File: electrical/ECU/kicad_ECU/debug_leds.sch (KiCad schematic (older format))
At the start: 6 parts

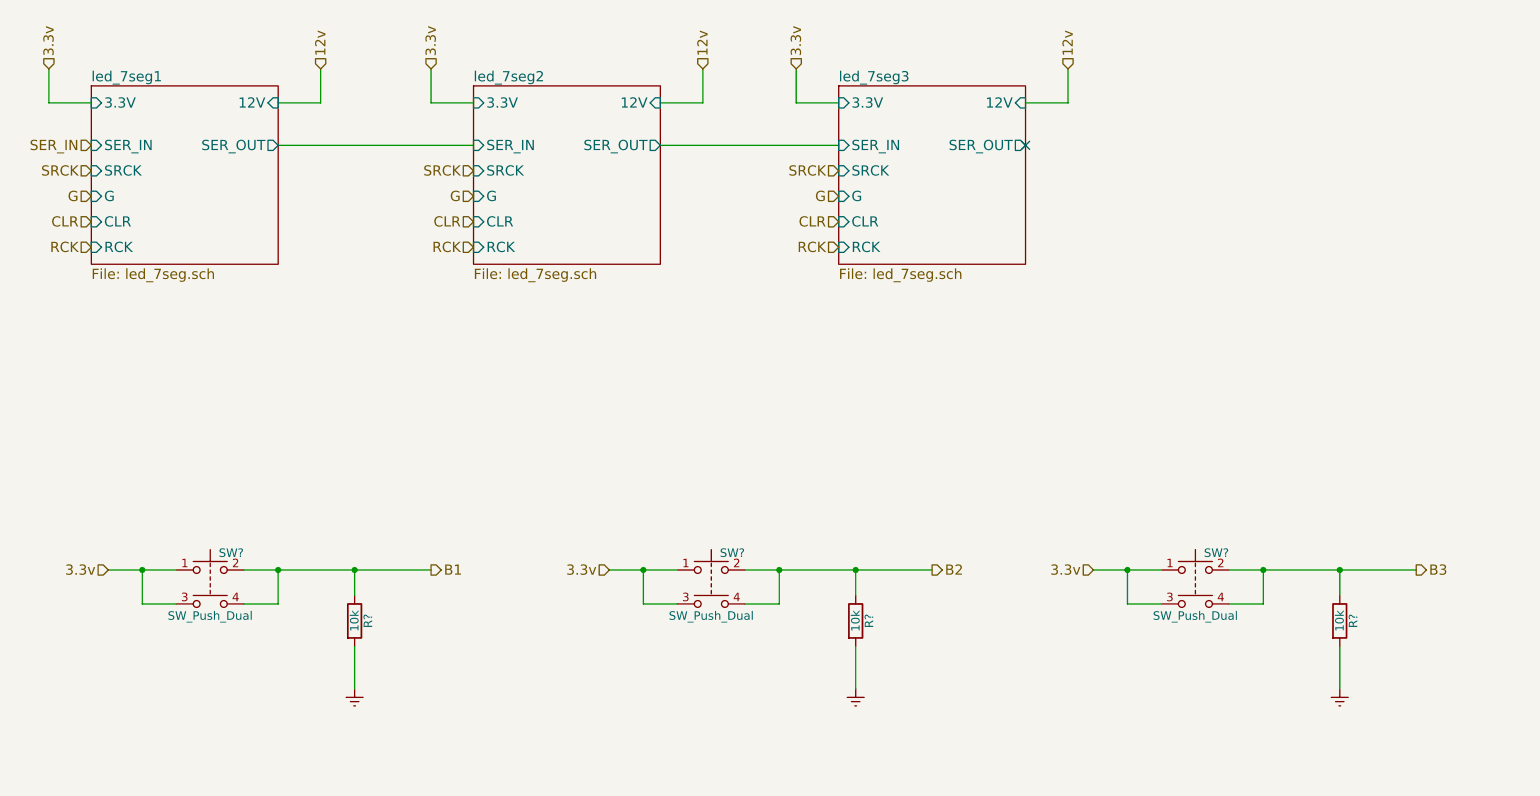
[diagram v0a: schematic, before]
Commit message: fixed some naming errors and initial round of double checking
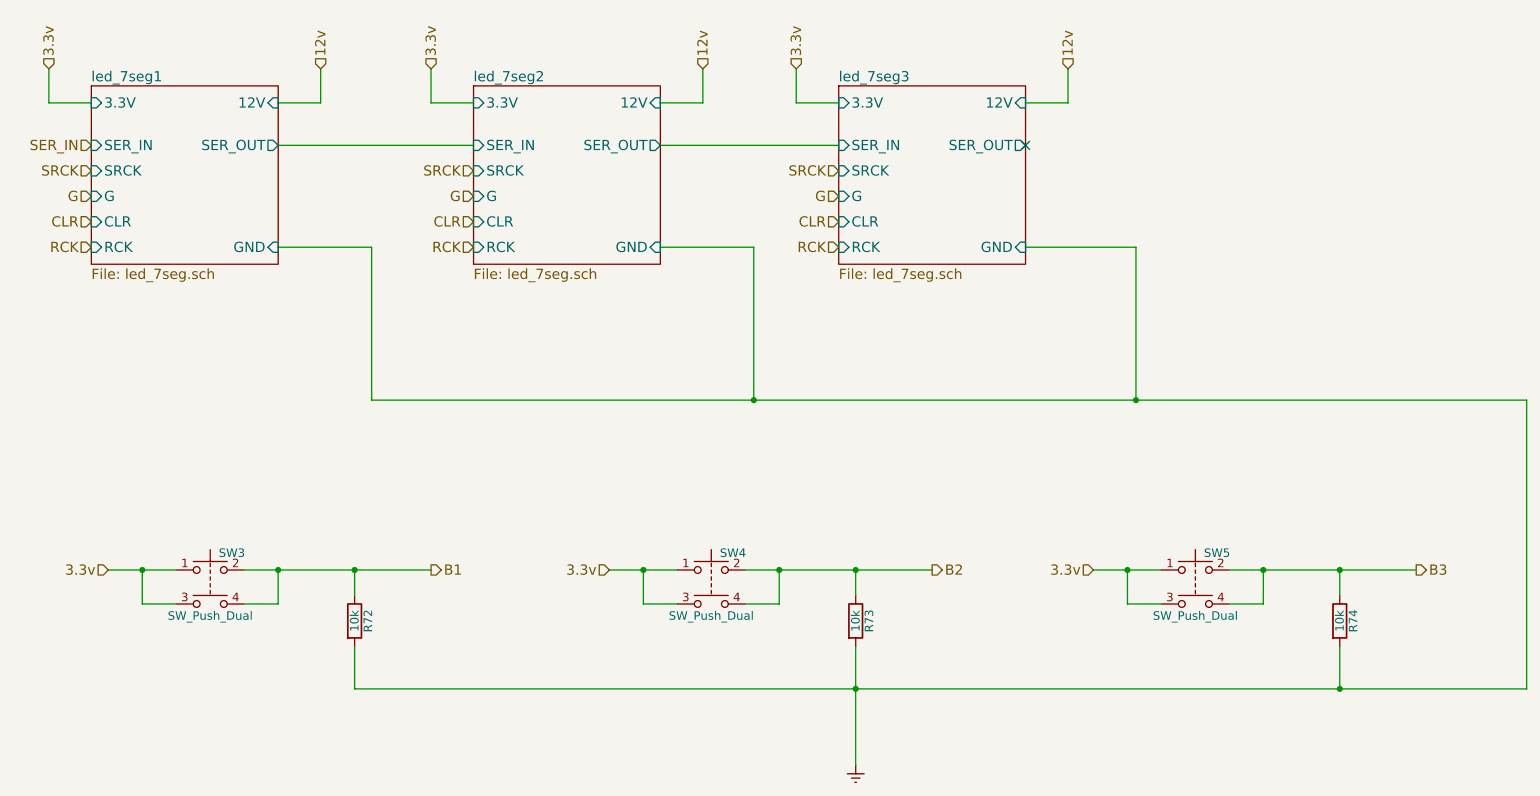
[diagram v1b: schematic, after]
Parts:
- gave numbers to parts that had none: 6
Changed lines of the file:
@@
 $Descr A4 11693 8268
 encoding utf-8
-Sheet 22 33
+Sheet 26 33
 Title "Display"
 Date ""
@@
 F8 "12V" I R 3700 1650 60
 F9 "SER_OUT" O R 3700 1900 60
+F10 "GND" I R 3700 2500 60
 $EndSheet
 $Sheet
@@
 F8 "12V" I R 5950 1650 60
 F9 "SER_OUT" O R 5950 1900 60
+F10 "GND" I R 5950 2500 60
 $EndSheet
 $Sheet
@@
 F8 "12V" I R 8100 1650 60
 F9 "SER_OUT" O R 8100 1900 60
+F10 "GND" I R 8100 2500 60
 $EndSheet
 Text HLabel 2350 1450 1    60   Input ~ 0
@@
 RCK
 $Comp
-L SW_Push_Dual SW?
+L SW_Push_Dual SW3
 U 1 1 597CD809
 P 3300 4400
-F 0 "SW?" H 3350 4500 50  0000 L CNN
+F 0 "SW3" H 3350 4500 50  0000 L CNN
 F 1 "SW_Push_Dual" H 3300 4130 50  0000 C CNN
 F 2 "" H 3300 4600 50  0001 C CNN
@@
 Connection ~ 3700 4400
 $Comp
-L R R?
+L R R72
 U 1 1 597CE2D4
 P 4150 4700
-F 0 "R?" V 4230 4700 50  0000 C CNN
+F 0 "R72" V 4230 4700 50  0000 C CNN
 F 1 "10k" V 4150 4700 50  0000 C CNN
 F 2 "" V 4080 4700 50  0001 C CNN
@@
 	1    0    0    -1
 $EndComp
-$Comp
-L Earth #PWR?
-U 1 1 597CE41C
-P 4150 5100
-F 0 "#PWR?" H 4150 4850 50  0001 C CNN
-F 1 "Earth" H 4150 4950 50  0001 C CNN
-F 2 "" H 4150 5100 50  0001 C CNN
-F 3 "" H 4150 5100 50  0001 C CNN
-	1    4150 5100
-	1    0    0    -1
-$EndComp
 Wire Wire Line
 	4150 4550 4150 4400
@@
 	4150 4850 4150 5100
 $Comp
-L SW_Push_Dual SW?
+L SW_Push_Dual SW4
 U 1 1 597CE671
 P 6250 4400
-F 0 "SW?" H 6300 4500 50  0000 L CNN
+F 0 "SW4" H 6300 4500 50  0000 L CNN
 F 1 "SW_Push_Dual" H 6250 4130 50  0000 C CNN
 F 2 "" H 6250 4600 50  0001 C CNN
@@
 Connection ~ 6650 4400
 $Comp
-L R R?
+L R R73
 U 1 1 597CE681
 P 7100 4700
-F 0 "R?" V 7180 4700 50  0000 C CNN
+F 0 "R73" V 7180 4700 50  0000 C CNN
 F 1 "10k" V 7100 4700 50  0000 C CNN
 F 2 "" V 7030 4700 50  0001 C CNN
@@
 	1    0    0    -1
 $EndComp
-$Comp
-L Earth #PWR?
-U 1 1 597CE687
-P 7100 5100
-F 0 "#PWR?" H 7100 4850 50  0001 C CNN
-F 1 "Earth" H 7100 4950 50  0001 C CNN
-F 2 "" H 7100 5100 50  0001 C CNN
-F 3 "" H 7100 5100 50  0001 C CNN
-	1    7100 5100
-	1    0    0    -1
-$EndComp
 Wire Wire Line
 	7100 4550 7100 4400
 Connection ~ 7100 4400
 Wire Wire Line
-	7100 4850 7100 5100
-$Comp
-L SW_Push_Dual SW?
+	7100 4850 7100 5550
+$Comp
+L SW_Push_Dual SW5
 U 1 1 597CE819
 P 9100 4400
-F 0 "SW?" H 9150 4500 50  0000 L CNN
+F 0 "SW5" H 9150 4500 50  0000 L CNN
 F 1 "SW_Push_Dual" H 9100 4130 50  0000 C CNN
 F 2 "" H 9100 4600 50  0001 C CNN
@@
 Connection ~ 9500 4400
 $Comp
-L R R?
+L R R74
 U 1 1 597CE829
 P 9950 4700
-F 0 "R?" V 10030 4700 50  0000 C CNN
+F 0 "R74" V 10030 4700 50  0000 C CNN
 F 1 "10k" V 9950 4700 50  0000 C CNN
 F 2 "" V 9880 4700 50  0001 C CNN
@@
 	1    0    0    -1
 $EndComp
-$Comp
-L Earth #PWR?
-U 1 1 597CE82F
-P 9950 5100
-F 0 "#PWR?" H 9950 4850 50  0001 C CNN
-F 1 "Earth" H 9950 4950 50  0001 C CNN
-F 2 "" H 9950 5100 50  0001 C CNN
-F 3 "" H 9950 5100 50  0001 C CNN
-	1    9950 5100
-	1    0    0    -1
-$EndComp
 Wire Wire Line
 	9950 4550 9950 4400
 Connection ~ 9950 4400
 Wire Wire Line
-	9950 4850 9950 5100
+	9950 5100 9950 4850
+$Comp
+L Earth #PWR66
+U 1 1 59922A45
+P 7100 5550
+F 0 "#PWR66" H 7100 5300 50  0001 C CNN
+F 1 "Earth" H 7100 5400 50  0001 C CNN
+F 2 "" H 7100 5550 50  0001 C CNN
+F 3 "" H 7100 5550 50  0001 C CNN
+	1    7100 5550
+	1    0    0    -1
+$EndComp
+Wire Wire Line
+	4150 5100 11050 5100
+Connection ~ 7100 5100
+Wire Wire Line
+	3700 2500 4250 2500
+Wire Wire Line
+	4250 2500 4250 3400
+Wire Wire Line
+	4250 3400 11050 3400
+Wire Wire Line
+	11050 3400 11050 5100
+Connection ~ 9950 5100
+Wire Wire Line
+	5950 2500 6500 2500
+Wire Wire Line
+	6500 2500 6500 3400
+Connection ~ 6500 3400
+Wire Wire Line
+	8100 2500 8750 2500
+Wire Wire Line
+	8750 2500 8750 3400
+Connection ~ 8750 3400
 $EndSCHEMATC
